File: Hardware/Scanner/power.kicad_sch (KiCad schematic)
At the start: 16 parts, among them J1 I2C ThroughHole, J3 I2C, J4 Interface, U10 AP2127N-1.8, U9 AP2127N-2.5

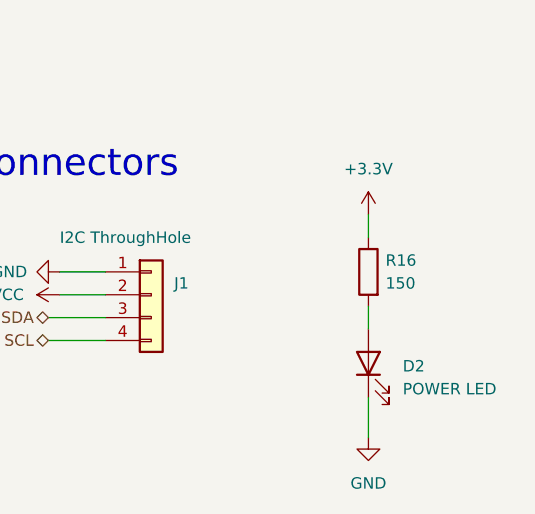
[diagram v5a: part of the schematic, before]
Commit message: updated red power led to a common lower value, dimmer power led shouldn't be an issue
Signed-off-by: lokimetasmith <lokimail@gmail.com>
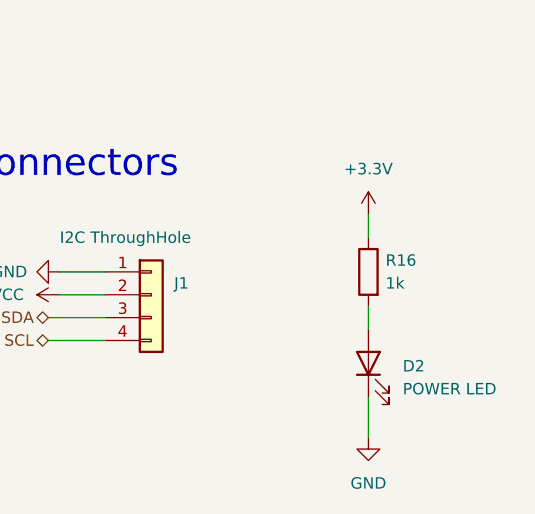
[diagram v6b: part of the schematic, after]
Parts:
- R16: value 150 -> 1k; digikey description (none) -> RES 1K OHM 1% 1/10W 0603; digikey part number (none) -> 311-1.00KHRCT-ND
- U10: digikey description (none) -> IC REG LINEAR 1.8V 300MA SOT23-3; digikey part number (none) -> AP2125N-1.8TRG1DICT-ND
- U9: digikey part number AP2127N-2.5TRG1DI-ND -> AP2120N-2.5TRG1DICT-ND
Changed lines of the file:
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@@
       (effects (font (size 1.27 1.27)) hide)
     )
-    (property "digikey part number" "AP2127N-2.5TRG1DI-ND" (at 33.655 108.585 0)
+    (property "digikey part number" "AP2120N-2.5TRG1DICT-ND" (at 33.655 108.585 0)
       (effects (font (size 1.27 1.27)) hide)
     )
@@
       (effects (font (size 1.27 1.27)) hide)
     )
+    (property "digikey description" "IC REG LINEAR 1.8V 300MA SOT23-3" (at 35.56 137.16 0)
+      (effects (font (size 1.27 1.27)) hide)
+    )
+    (property "digikey part number" "AP2125N-1.8TRG1DICT-ND" (at 35.56 137.16 0)
+      (effects (font (size 1.27 1.27)) hide)
+    )
     (pin "1")
     (pin "2")
@@
       (effects (font (size 1.27 1.27)) (justify right))
     )
-    (property "Value" "150" (at 222.885 138.4299 0)
+    (property "Value" "1k" (at 222.885 138.4299 0)
       (effects (font (size 1.27 1.27)) (justify right))
     )
@@
       (effects (font (size 1.27 1.27)) hide)
     )
+    (property "digikey description" "RES 1K OHM 1% 1/10W 0603" (at 220.98 137.16 0)
+      (effects (font (size 1.27 1.27)) hide)
+    )
+    (property "digikey part number" "311-1.00KHRCT-ND" (at 220.98 137.16 0)
+      (effects (font (size 1.27 1.27)) hide)
+    )

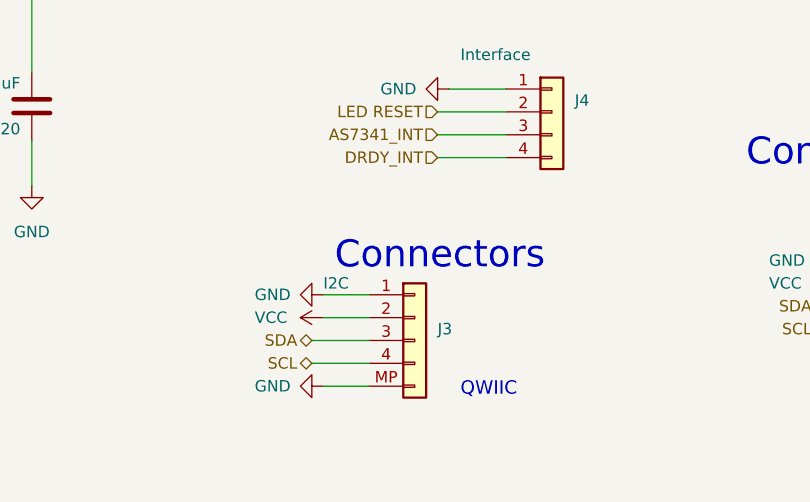
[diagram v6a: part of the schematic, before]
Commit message: added missing QUICC connector
Signed-off-by: lokimetasmith <lokimail@gmail.com>
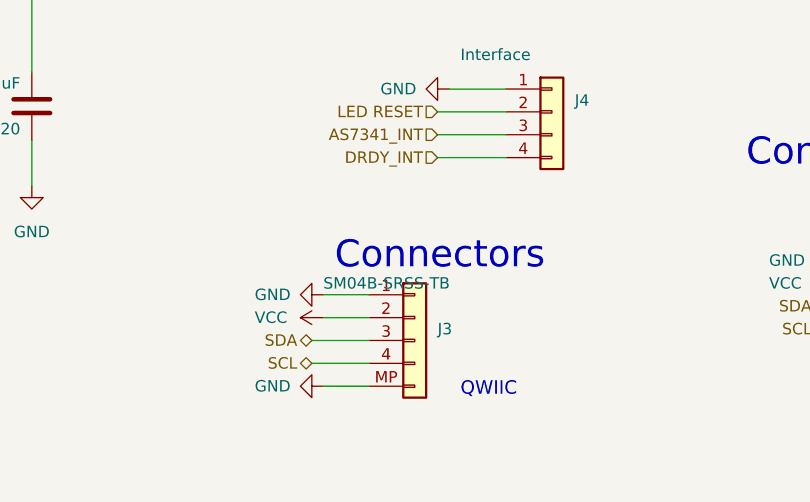
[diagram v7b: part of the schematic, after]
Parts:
- J3: value I2C -> SM04B-SRSS-TB; digikey description (none) -> SM04B-SRSS-TB; digikey part number (none) -> 455-SM04B-SRSS-TBCT-ND
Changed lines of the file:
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@@
       (effects (font (size 1.27 1.27)) (justify left))
     )
-    (property "Value" "I2C" (at 129.54 139.7 0)
+    (property "Value" "SM04B-SRSS-TB" (at 129.54 139.7 0)
       (effects (font (size 1.27 1.27)) (justify left))
     )
@@
       (effects (font (size 1.27 1.27)) hide)
     )
+    (property "digikey description" "SM04B-SRSS-TB" (at 139.7 146.05 0)
+      (effects (font (size 1.27 1.27)) hide)
+    )
+    (property "digikey part number" "455-SM04B-SRSS-TBCT-ND" (at 139.7 146.05 0)
+      (effects (font (size 1.27 1.27)) hide)
+    )

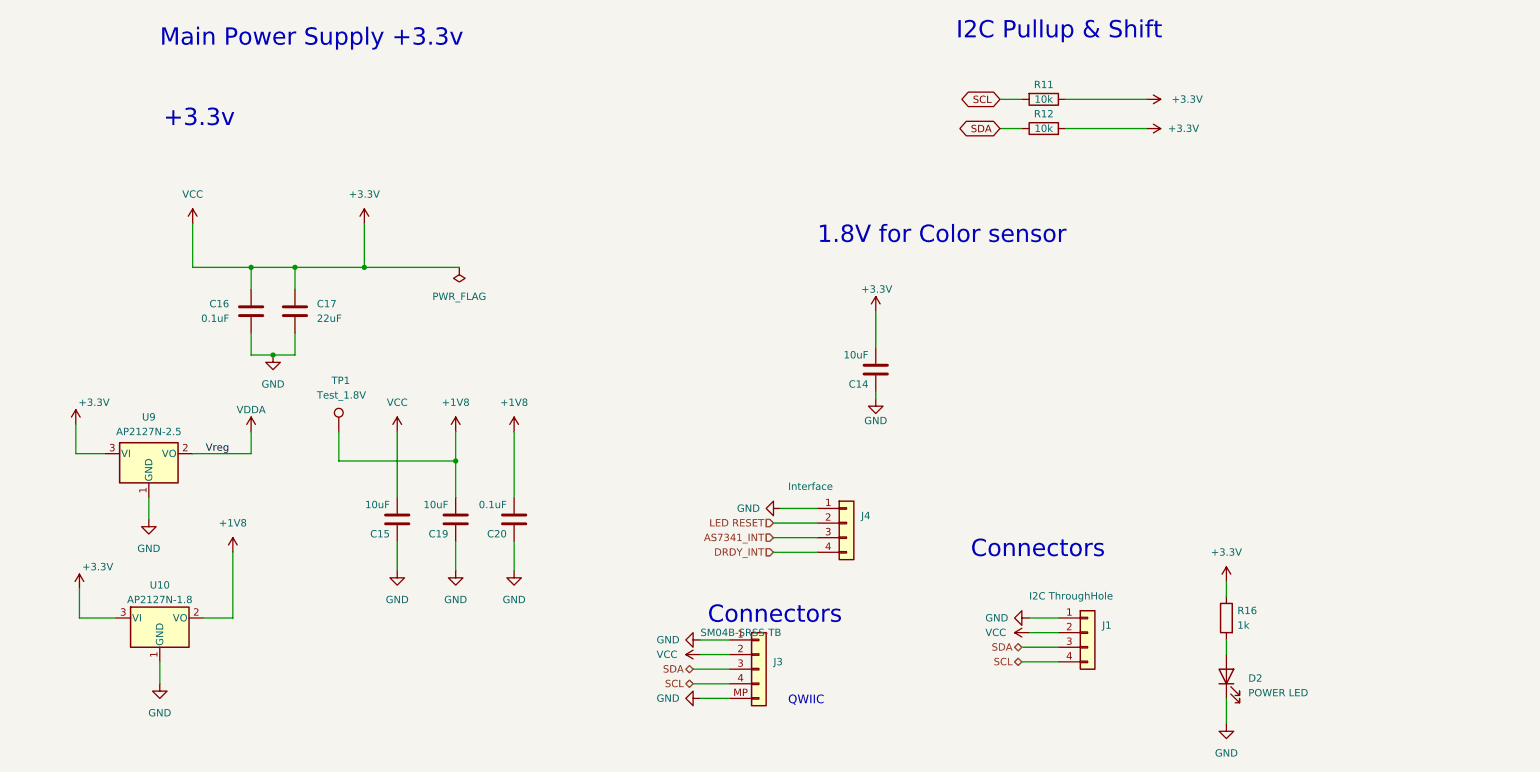
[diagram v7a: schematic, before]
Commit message: added decoupling capactitors, added footprint for 3d model, need to verify new footprint
Signed-off-by: lokimetasmith <lokimail@gmail.com>
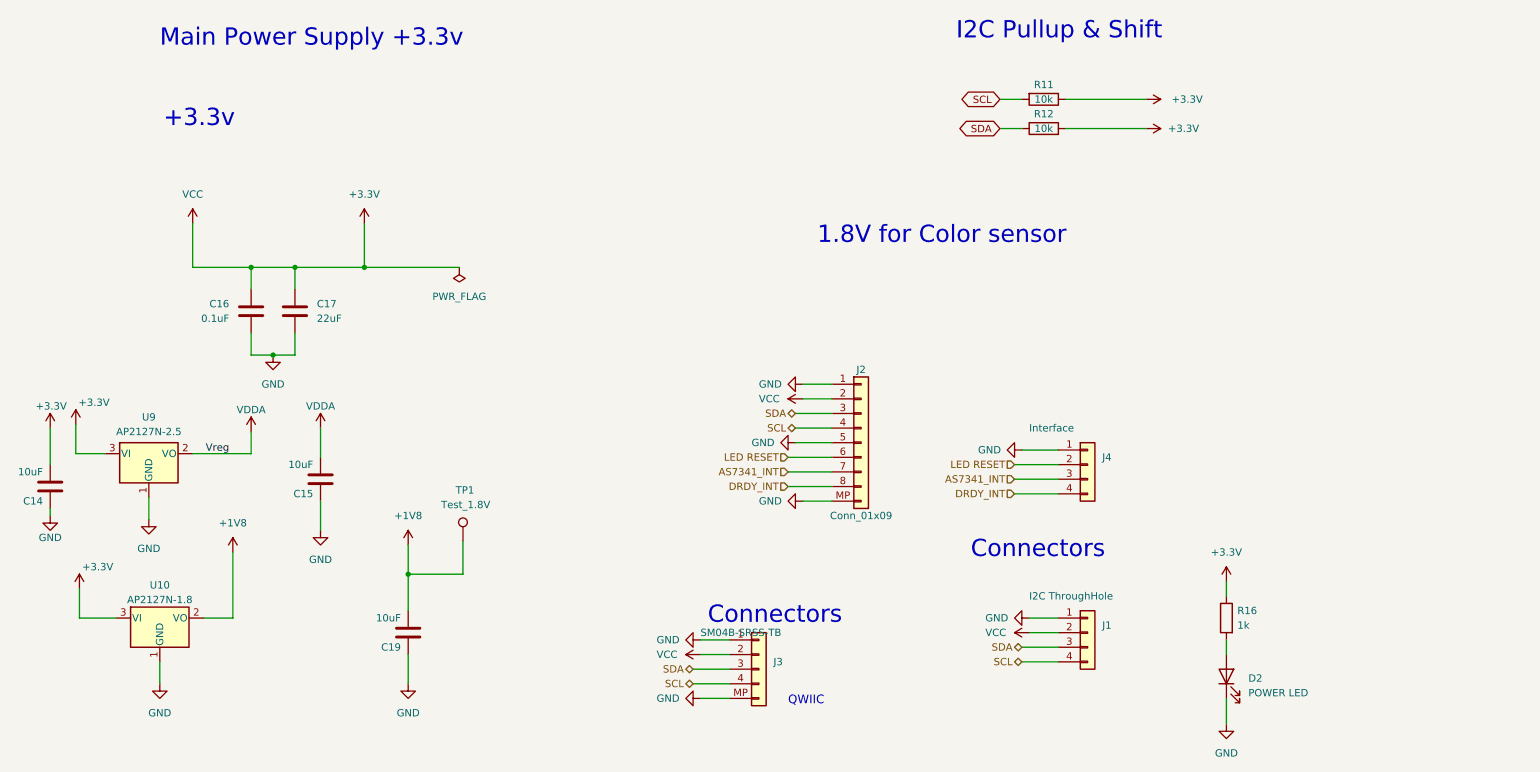
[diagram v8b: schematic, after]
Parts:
- removed C20: 0.1uF, Capacitor_SMD:C_0603_1608Metric_Pad1.08x0.95mm_HandSolder, symbol Device:C
- added J2: Conn_01x09, round_module:round_notch, symbol Connector_Generic:Conn_01x09
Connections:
- net +3.3V: now also J2.2 (Pin_2); no longer C15.2
- net AS7341_INT: now also J2.7 (Pin_7)
- net DRDY_INT: now also J2.8 (Pin_8)
- net GND: now also J2.1 (Pin_1), J2.5 (Pin_5), J2.MP
- net LED RESET: now also J2.6 (Pin_6)
- net SCL: now also J2.4 (Pin_4)
- net SDA: now also J2.3 (Pin_3)
- net VDDA: now also C15.2
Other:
- moved on the sheet: C14, C15, C19, J4, TP1
